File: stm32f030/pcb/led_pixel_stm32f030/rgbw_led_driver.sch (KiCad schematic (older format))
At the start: 25 parts

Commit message: designed a first draft of the backplane of the dynamic adressing LED Pixels
started with pcb design of the STM32 version
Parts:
- gave numbers to parts that had none: 25

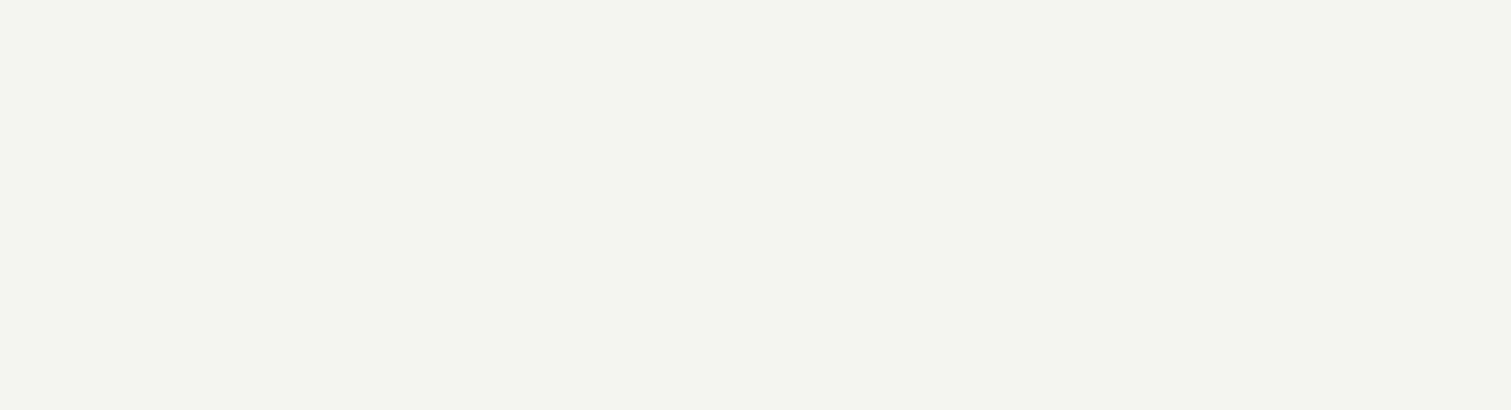
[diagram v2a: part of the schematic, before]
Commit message: added mounting holes
added a lot of capacitors (there was some room left ;) )

layout nearly finished
logos are missing ;)
not much work left I think
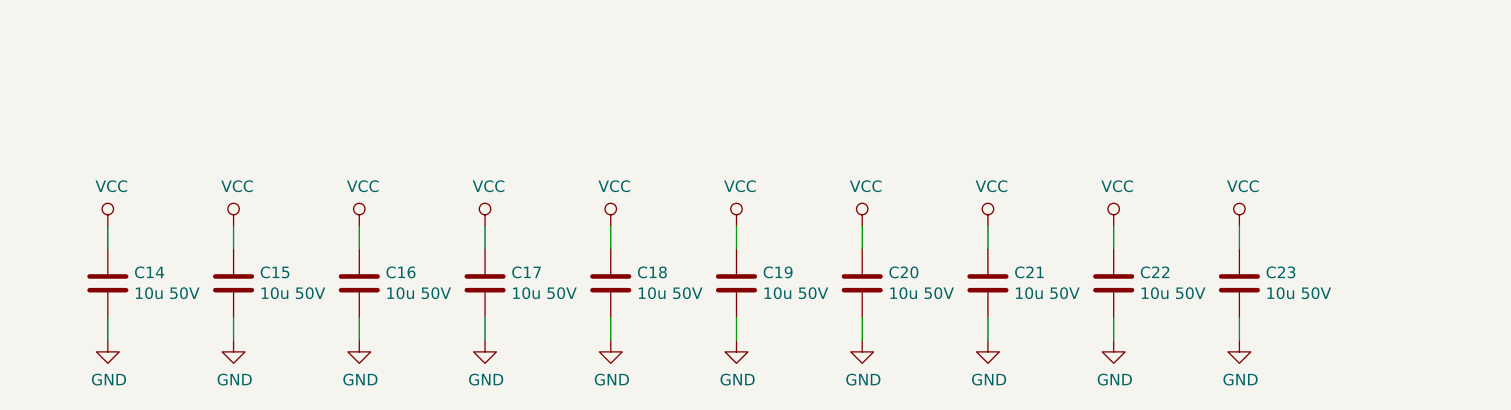
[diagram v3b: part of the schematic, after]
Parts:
- added C14, C15, C16, C17, C18, C19, C20, C21, C22, C23: 10u 50V, Capacitors_SMD:C_1210, symbol C
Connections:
- net GND: now also C14.2, C15.2, C16.2, C17.2, C18.2, C19.2, C20.2, C21.2, C22.2, C23.2
- net VCC: now also C14.1, C15.1, C16.1, C17.1, C18.1, C19.1, C20.1, C21.1, C22.1, C23.1

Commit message: updraded to revision V1.1
Now the cooling pad of the LED is isolated from the ground plane.
Unfortunately there will be less cooling than before, but the LEDs to use have a stupid connection...
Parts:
- D5: footprint proz_led:LED_SMD_RGBW_4W -> proz_led:LED_SMD_RGBW_4W_ISOLATED
